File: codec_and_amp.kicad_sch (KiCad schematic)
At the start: 32 parts, among them J1 Conn_01x08, J2 Conn_01x06, U1 TLV320AIC3206IRSBR, U4 FSA2275UMX, U6 MIC5504-1.8YM5, U7 TPD4E02B04DQAR, U8 TPD4E02B04DQAR

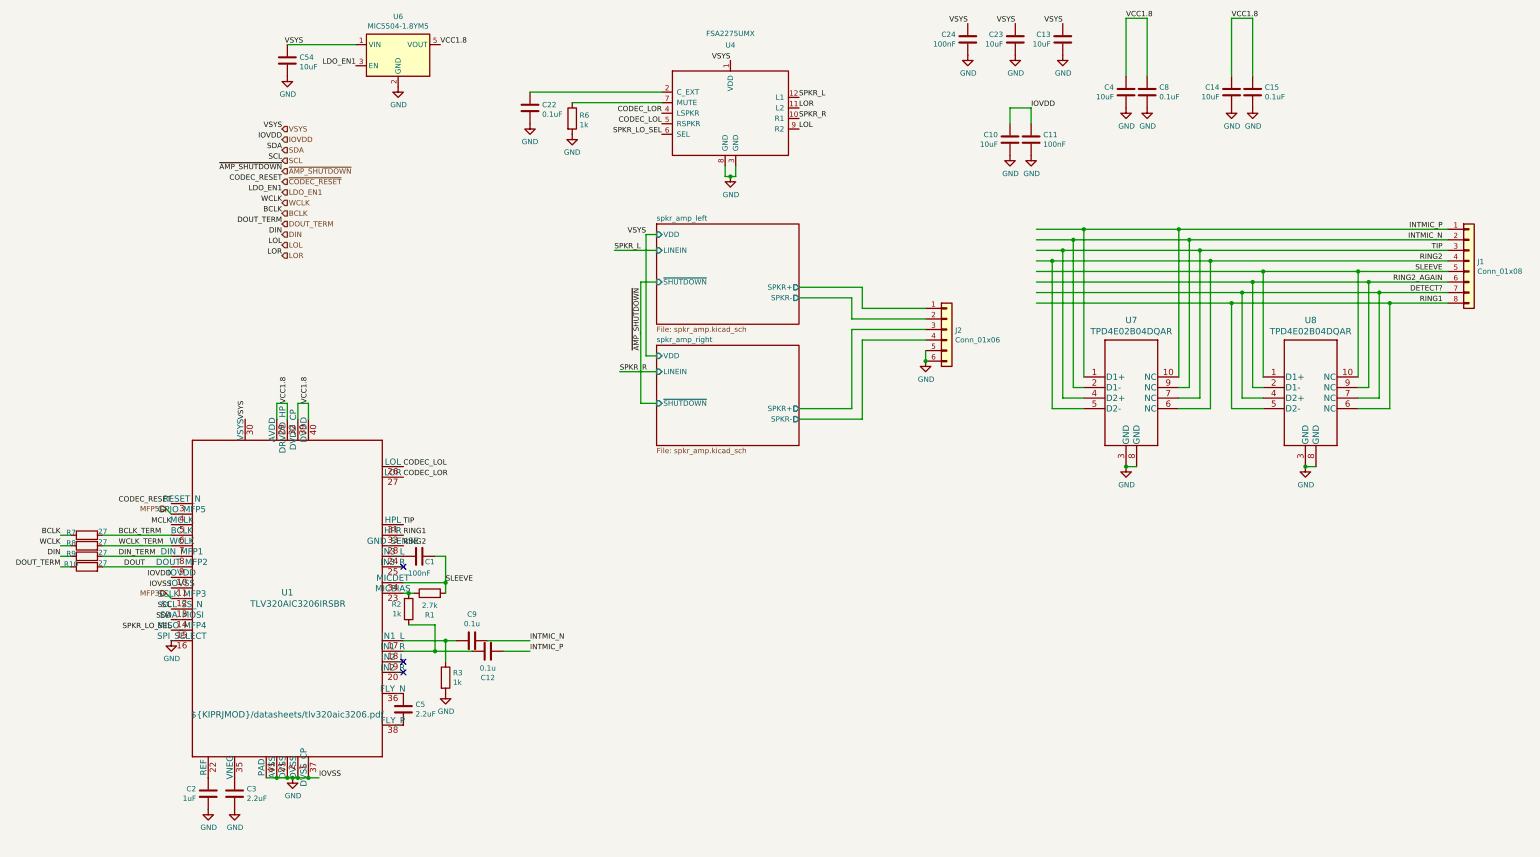
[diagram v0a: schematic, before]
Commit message: Even more testpoints!
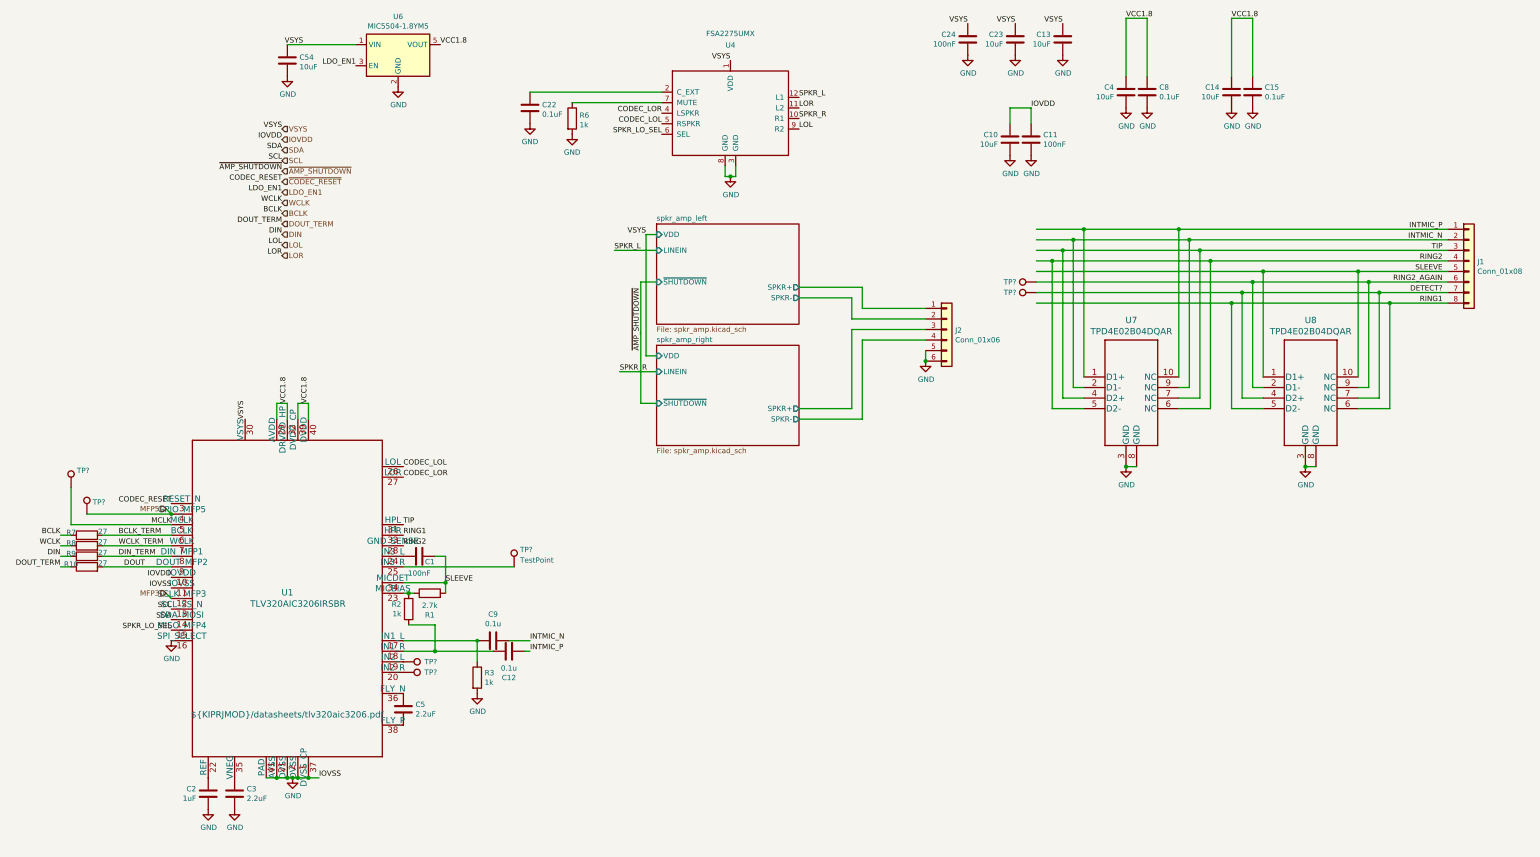
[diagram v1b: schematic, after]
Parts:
- added TP? (x7): TestPoint, footprints:testpoint_small, symbol Connector:TestPoint
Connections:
- net DETECT?: now also TP?.1
- net MCLK: now also TP?.1
- net MFP5: now also TP?.1
- net RING2_AGAIN: now also TP?.1
- net at U1.19 (IN2_L): now also TP?.1
- net at U1.20 (IN2_R): now also TP?.1
- net at U1.25 (IN3_R): now also TP?.1
- no-connect marks 3 -> 0
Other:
- moved on the sheet: C12, C9, R3

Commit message: Flip J4 to back of board to reduce overall thickness in that area; re-route a whole bunch of signals to accomodate that.
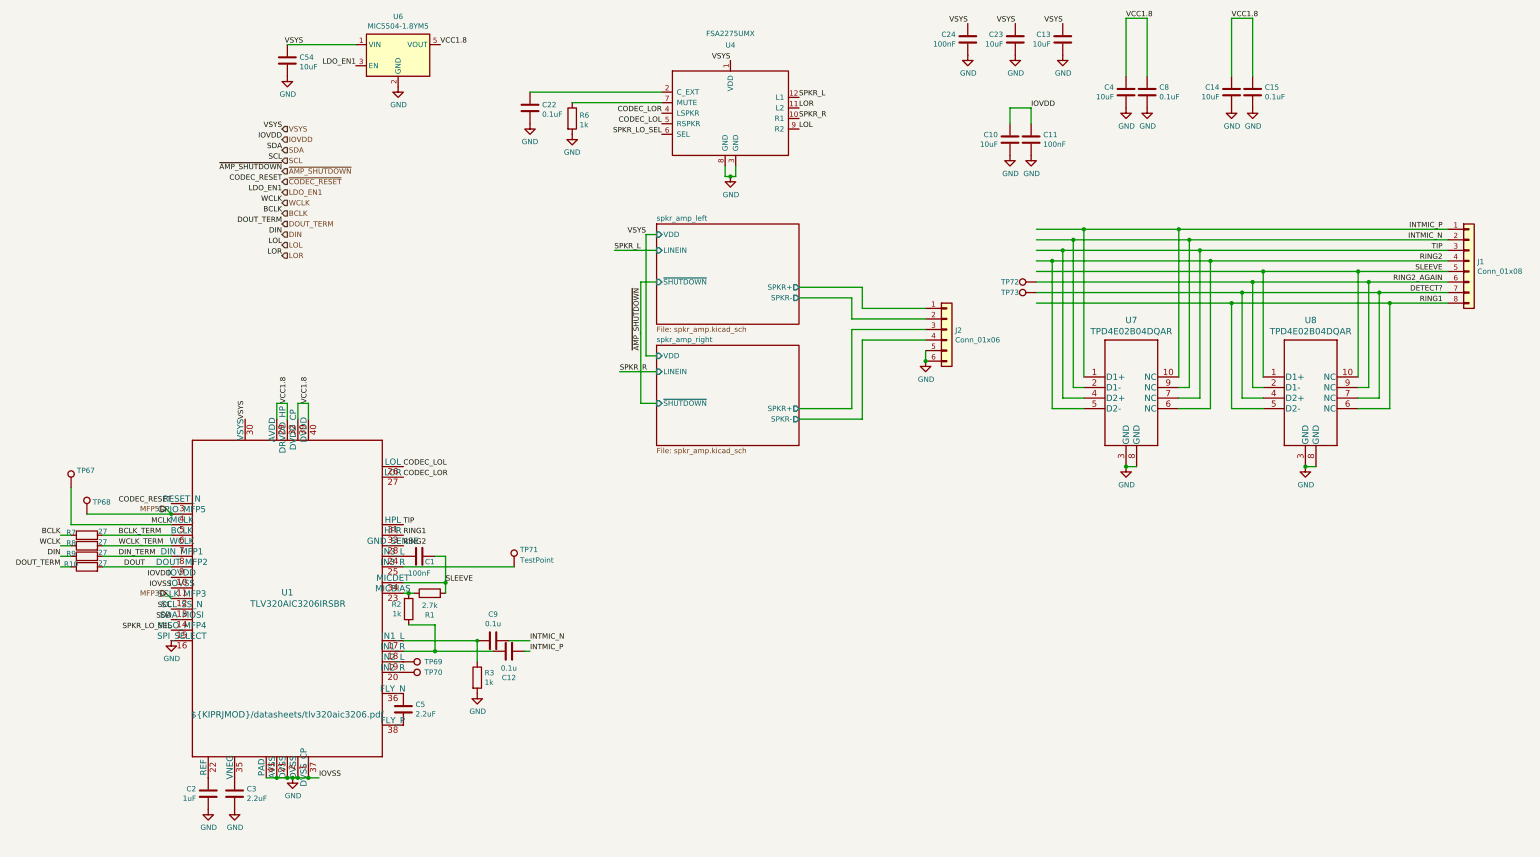
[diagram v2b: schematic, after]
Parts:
- gave numbers to parts that had none: 7
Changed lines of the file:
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@@
   (symbol (lib_id "Connector:TestPoint") (at 265.43 105.41 90) (unit 1)
     (in_bom yes) (on_board yes)
-    (property "Reference" "TP?" (id 0) (at 259.08 105.41 90))
+    (property "Reference" "TP73" (id 0) (at 259.08 105.41 90))
     (property "Value" "TestPoint" (id 1) (at 262.128 103.6121 90)
       (effects (font (size 1.27 1.27)) hide)
@@
   (symbol (lib_id "Connector:TestPoint") (at 113.03 194.31 270) (unit 1)
     (in_bom yes) (on_board yes)
-    (property "Reference" "TP?" (id 0) (at 118.11 194.31 90)
+    (property "Reference" "TP69" (id 0) (at 118.11 194.31 90)
       (effects (font (size 1.27 1.27)) (justify left))
     )
@@
   (symbol (lib_id "Connector:TestPoint") (at 265.43 102.87 90) (unit 1)
     (in_bom yes) (on_board yes)
-    (property "Reference" "TP?" (id 0) (at 259.08 102.87 90))
+    (property "Reference" "TP72" (id 0) (at 259.08 102.87 90))
     (property "Value" "TestPoint" (id 1) (at 262.128 101.0721 90)
       (effects (font (size 1.27 1.27)) hide)
@@
   (symbol (lib_id "Connector:TestPoint") (at 36.83 158.75 0) (unit 1)
     (in_bom yes) (on_board yes) (fields_autoplaced)
-    (property "Reference" "TP?" (id 0) (at 38.227 155.8818 0)
+    (property "Reference" "TP68" (id 0) (at 38.227 155.8818 0)
       (effects (font (size 1.27 1.27)) (justify left))
     )
@@
   (symbol (lib_id "Connector:TestPoint") (at 113.03 196.85 270) (unit 1)
     (in_bom yes) (on_board yes)
-    (property "Reference" "TP?" (id 0) (at 118.11 196.85 90)
+    (property "Reference" "TP70" (id 0) (at 118.11 196.85 90)
       (effects (font (size 1.27 1.27)) (justify left))
     )
@@
   (symbol (lib_id "Connector:TestPoint") (at 33.02 152.4 0) (unit 1)
     (in_bom yes) (on_board yes)
-    (property "Reference" "TP?" (id 0) (at 34.417 148.2633 0)
+    (property "Reference" "TP67" (id 0) (at 34.417 148.2633 0)
       (effects (font (size 1.27 1.27)) (justify left))
     )
@@
   (symbol (lib_id "Connector:TestPoint") (at 139.7 171.45 0) (unit 1)
     (in_bom yes) (on_board yes)
-    (property "Reference" "TP?" (id 0) (at 141.097 167.3133 0)
-      (effects (font (size 1.27 1.27)) (justify left))
-    )
+    (property "Reference" "TP71" (id 0) (at 141.097 167.3133 0)
+      (effects (font (size 1.27 1.27)) (justify left))
+    )

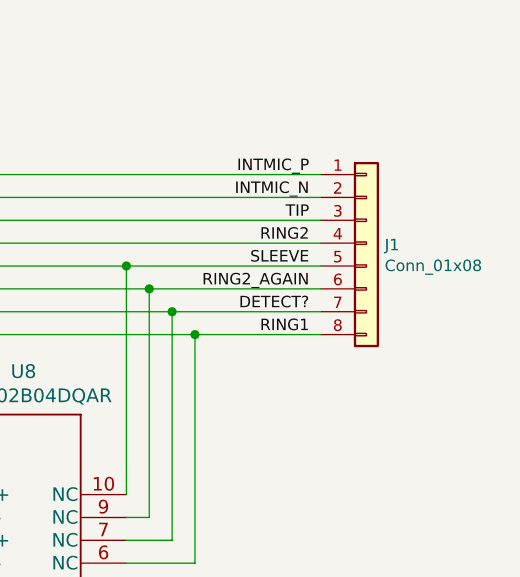
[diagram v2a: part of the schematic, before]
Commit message: Wire GT9110 INT pin to a GPIO, wire ARM_RST and Wake pins to test points instead of GPIOs. Add lots of test points, and footprints for status/power LEDs.
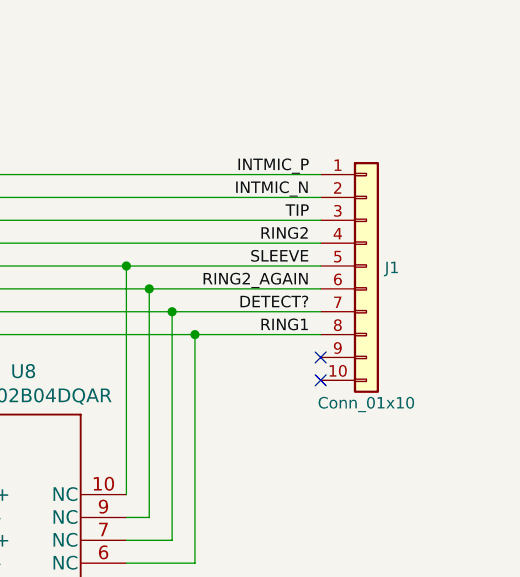
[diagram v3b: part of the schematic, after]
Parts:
- J1: value Conn_01x08 -> Conn_01x10; symbol Connector_Generic:Conn_01x08 -> Connector_Generic:Conn_01x10
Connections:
- no-connect marks 0 -> 2
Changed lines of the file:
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@@
   (junction (at 114.3 177.8) (diameter 1.016) (color 0 0 0 0)
   )
+  (no_connect (at 364.49 110.49))
+  (no_connect (at 364.49 113.03))
   (wire (pts (xy 265.43 97.79) (xy 269.24 97.79))
     (stroke (width 0) (type solid) (color 0 0 0 0))
@@
     (effects (font (size 1.27 1.27)) (justify right))
   )
-  (symbol (lib_id "Connector_Generic:Conn_01x08") (at 369.57 97.79 0) (unit 1)
+  (symbol (lib_id "Connector_Generic:Conn_01x10") (at 369.57 100.33 0) (unit 1)
     (in_bom yes) (on_board yes)
-    (property "Reference" "J1" (id 0) (at 371.602 97.9932 0)
+    (property "Reference" "J1" (id 0) (at 371.602 100.5332 0)
       (effects (font (size 1.27 1.27)) (justify left))
     )
-    (property "Value" "Conn_01x08" (id 1) (at 371.602 100.3046 0)
-      (effects (font (size 1.27 1.27)) (justify left))
-    )
-    (property "Footprint" "footprints:FF18-8A-R11AD-B-3H" (id 2) (at 369.57 97.79 0)
+    (property "Value" "Conn_01x10" (id 1) (at 369.57 115.57 0))
+    (property "Footprint" "footprints:FF18-8A-R11AD-B-3H" (id 2) (at 369.57 100.33 0)
       (effects (font (size 1.27 1.27)) hide)
     )
-    (property "Datasheet" "~" (id 3) (at 369.57 97.79 0)
+    (property "Datasheet" "~" (id 3) (at 369.57 100.33 0)
       (effects (font (size 1.27 1.27)) hide)
     )
     (pin "1")
+    (pin "10")
     (pin "2")
     (pin "3")
@@
     (pin "7")
     (pin "8")
+    (pin "9")
   )
   (symbol (lib_id "Device:R") (at 119.38 177.8 90) (unit 1)
